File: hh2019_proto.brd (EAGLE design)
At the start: 263.1 x 150 mm, 146 parts, among them IC1 CP210X_USB_UART, IC2 AP2114H, IC4 TP4056, J1 PJ-313D, Q1 MMBT2222A, Q3 MMBT2222A, Q4 MMBT2222A, Q5 SI1304 BDL, U1 MPR121QR2, U2 ESP32-WROVER-I, U3 PCM5102A, X4 JST-PH3

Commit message: Placed major components, working on passives
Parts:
- removed C31: 100n, hh2019_proto:C0603-DASHES
- moved Q3 265.5 mm to (-135.9, 67.3)
- moved R22 262.2 mm to (-133.3, 64.8), turned to 180 degrees
- moved R16 261.1 mm to (-133.3, 73.7), turned to 0 degrees
- moved R15 258.0 mm to (-138.4, 69.8), turned to 90 degrees
- moved R18 255.2 mm to (-133.3, 69.8), turned to 270 degrees
- moved Q4 253.3 mm to (-135.9, 72.4), turned to 0 degrees
- moved IC4 252.3 mm to (-104.1, 74.9), turned to 180 degrees
- moved C28 223.6 mm to (-135.9, 99.1), turned to 90 degrees
- moved C29 216.0 mm to (-134.6, 99.1), turned to 90 degrees
- moved C37 190.2 mm to (135.9, 130.8)
- moved R20 190.2 mm to (135.9, 138.4)
- moved R21 190.2 mm to (135.9, 142.2)
- moved C16 190.2 mm to (137.2, 138.4)
- moved C38 190.2 mm to (143.5, 129.5)
- moved C39 190.2 mm to (153.7, 120.7)
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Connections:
- net GND: no longer C31.1
- net N$43: no longer C31.2
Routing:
- net WS2812_POWER: track 0.00 -> 68.8 mm
- net ESP32_FLASH: track 0.00 -> 60.5 mm, vias 0 -> 2
- net CHRG_STAT: track 4.52 -> 44.3 mm, vias 2 -> 4
- net GND: track 23.2 -> 61.7 mm, vias 7 -> 28
- net VBAT: track 0.00 -> 25.9 mm
- net WS2812_DATA: track 0.00 -> 23.8 mm, vias 0 -> 2
- net USB_DP_CON: track 0.00 -> 12.9 mm, vias 0 -> 2
- net USB_DN_CON: track 0.00 -> 11.7 mm
- net N$4: track 0.00 -> 9.75 mm
- net N$3: track 0.00 -> 9.75 mm
- net N$2: track 0.00 -> 9.75 mm
- net N$19: track 0.00 -> 9.75 mm
- net N$43: track 0.00 -> 9.15 mm
- net N$42: track 0.00 -> 8.39 mm
- net N$53: track 0.00 -> 7.33 mm
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
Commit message: Routing tracks
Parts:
- moved C27 369.4 mm to (-101.7, 78.8), turned to 0 degrees
- moved C22 366.0 mm to (-102.8, 81.4), turned to 270 degrees
- moved C17 359.8 mm to (-102.8, 85.2), turned to 270 degrees
- moved C26 354.5 mm to (-102.8, 90.2), turned to 270 degrees
- moved C30 349.1 mm to (-102.8, 95.3), turned to 270 degrees
- moved IC2 337.7 mm to (-97.8, 92.8), turned to 0 degrees
- moved C15 334.1 mm to (-97.8, 86.4), turned to 180 degrees
- moved C14 331.6 mm to (-97.8, 83.9), turned to 180 degrees
- moved C18 329.4 mm to (-97.8, 80.8), turned to 180 degrees
- moved R19 274.3 mm to (-121.9, 129.5)
- moved C19 270.5 mm to (-119.4, 129.5)
- moved C21 266.7 mm to (-116.8, 129.5)
- moved C33 262.9 mm to (-114.3, 129.5)
- moved C36 259.1 mm to (-114.3, 125.7)
- moved C32 259.1 mm to (-111.8, 129.5)
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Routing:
- net GND: track 61.7 -> 92.4 mm, vias 28 -> 33
- net VCC: track 2.85 -> 31.5 mm, vias 0 -> 2
- net VGH: track 0.00 -> 16.6 mm, vias 0 -> 2
- net VGL: track 0.00 -> 13.5 mm, vias 0 -> 2
- net VSL: track 0.00 -> 10.1 mm
- net VCOM: track 0.00 -> 9.84 mm, vias 0 -> 2
- net PREVGL: track 0.00 -> 8.85 mm, vias 0 -> 2
- net PREVGH: track 0.00 -> 8.55 mm
- net RESE: track 0.00 -> 8.42 mm, vias 0 -> 2
- net VSH: track 0.00 -> 6.55 mm
- net VBAT: track 25.9 -> 20.0 mm, vias 0 -> 2
- net +5V: track 0.00 -> 5.56 mm
- net ESP32_FLASH: track 60.5 -> 61.6 mm
- net ESP32_!RESET: track 44.4 -> 45.5 mm, vias 0 -> 2
- net I2C_SDA: track 69.4 -> 70.3 mm
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
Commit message: Added most non-bypass passives
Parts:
- moved Q5 270.6 mm to (-115.6, 121.9), turned to 270 degrees
- moved C23 264.3 mm to (-113.0, 86.4), turned to 0 degrees
- moved C24 264.0 mm to (-113.0, 82.5), turned to 180 degrees
- moved R30 262.7 mm to (-113.0, 78.7), turned to 0 degrees
- moved R32 262.5 mm to (-113.0, 74.9), turned to 0 degrees
- moved L1 261.8 mm to (-106.8, 120.0)
- moved R29 258.6 mm to (-110.5, 66.0), turned to 180 degrees
- moved R35 258.6 mm to (-110.5, 63.5), turned to 0 degrees
- moved SJ3 258.6 mm to (-110.5, 61.0), turned to 180 degrees
- moved C25 257.8 mm to (-106.7, 124.5), turned to 90 degrees
- moved D9 256.6 mm to (-109.2, 129.5)
- moved D8 256.5 mm to (-111.8, 125.7), turned to 90 degrees
- moved D7 252.8 mm to (-110.5, 121.9), turned to 0 degrees
- moved R36 248.2 mm to (-106.7, 68.6), turned to 0 degrees
- moved C34 244.9 mm to (-97.4, 78.0), turned to 0 degrees
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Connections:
- new net BAT: C34.1, F2.1, IC4.5, X4.3
- net VBAT: no longer C34.1, F2.1, IC4.5, X4.3
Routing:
- net +5V: track 5.56 -> 108.2 mm, vias 0 -> 4
- net N$50: track 0.00 -> 78.4 mm, vias 0 -> 4
- net N$11: track 0.00 -> 69.5 mm, vias 0 -> 4
- net N$10: track 0.00 -> 65.3 mm, vias 0 -> 4
- net WS2812_POWER: track 68.8 -> 132.2 mm, vias 0 -> 4
- net I2S_SCK: track 0.00 -> 51.5 mm, vias 0 -> 2
- net ESP32_TX: track 5.49 -> 46.1 mm, vias 0 -> 2
- net ESP32_RX: track 5.78 -> 44.6 mm, vias 0 -> 2
- net I2S_SD: track 0.00 -> 37.9 mm, vias 0 -> 2
- net I2S_WS: track 0.00 -> 36.6 mm, vias 0 -> 2
- net GND: track 92.4 -> 126.3 mm, vias 33 -> 43
- net I2C_INT: track 68.4 -> 98.2 mm
- net LCD_VDD: track 0.00 -> 18.7 mm, vias 0 -> 2
- net ESP32_FLASH: track 61.6 -> 80.2 mm
- net BAT: track 0.00 -> 18.6 mm, vias 0 -> 2
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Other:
- board text removed: "+3V3"
- board text removed: "3V3_SWITCHED"
- board text removed: "ESP32_!RESET"
- board text removed: "ESP32_FLASH"
- board text removed: "I2C_SCL"
- board text removed: "I2C_SDA"
- board text removed: "WS2812_POWER"

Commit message: All but the last handful passives placed and routed
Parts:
- moved C16 173.1 mm to (-111.8, 95.2), turned to 270 degrees
- moved R20 168.1 mm to (-109.2, 95.2), turned to 90 degrees
- moved R21 163.1 mm to (-106.7, 95.2), turned to 270 degrees
- moved R23 153.1 mm to (-113.0, 100.3)
- moved R24 153.1 mm to (-109.2, 100.3)
- moved R12 149.4 mm to (-109.2, 108.0), turned to 90 degrees
- moved D6 147.0 mm to (-111.8, 108.0), turned to 0 degrees
- moved C9 105.6 mm to (-146.1, 133.3), turned to 270 degrees
- moved D1 102.9 mm to (-146.1, 138.4)
- moved C11 98.5 mm to (-146.1, 128.3), turned to 270 degrees
- moved C20 95.3 mm to (-22.9, 94.0)
- moved C37 95.3 mm to (-40.6, 109.2)
- moved C39 95.3 mm to (-22.9, 99.1)
- moved C40 95.3 mm to (-57.1, 99.1)
- moved C46 95.3 mm to (-22.9, 96.5)
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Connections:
- net N$8 renamed RST
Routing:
- net VDD: track 14.9 -> 87.5 mm, vias 2 -> 7
- net VBAT_SENSE: track 0.00 -> 35.9 mm
- net GND: track 126.3 -> 160.1 mm, vias 43 -> 51
- net VUSB_SENSE: track 0.00 -> 25.5 mm, vias 0 -> 2
- net GDR: track 0.00 -> 24.9 mm, vias 0 -> 2
- net RESE: track 8.42 -> 29.4 mm, vias 2 -> 4
- net +5V: track 108.2 -> 126.8 mm
- net LDO0: track 0.00 -> 15.3 mm, vias 0 -> 2
- net VBAT: track 3.79 -> 18.4 mm
- net VNEG: track 0.00 -> 14.3 mm, vias 0 -> 2
- net I2C_SCL: track 68.7 -> 80.9 mm, vias 2 -> 3
- net CAPP: track 0.00 -> 10.3 mm
- net CAPM: track 0.00 -> 9.82 mm
- net I2C_SDA: track 70.3 -> 78.7 mm, vias 2 -> 3
- net BAT: track 18.6 -> 25.8 mm
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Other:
- board text added: "Power"

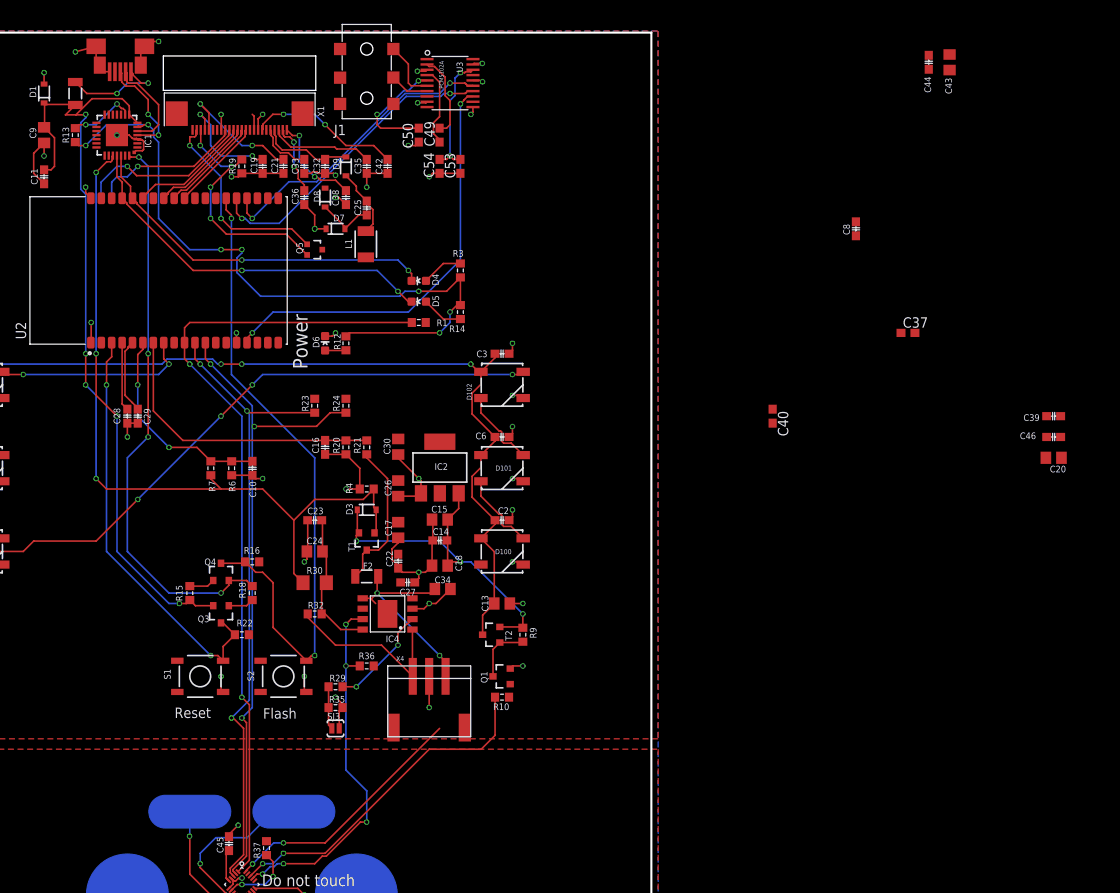
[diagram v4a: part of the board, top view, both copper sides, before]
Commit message: All components placed
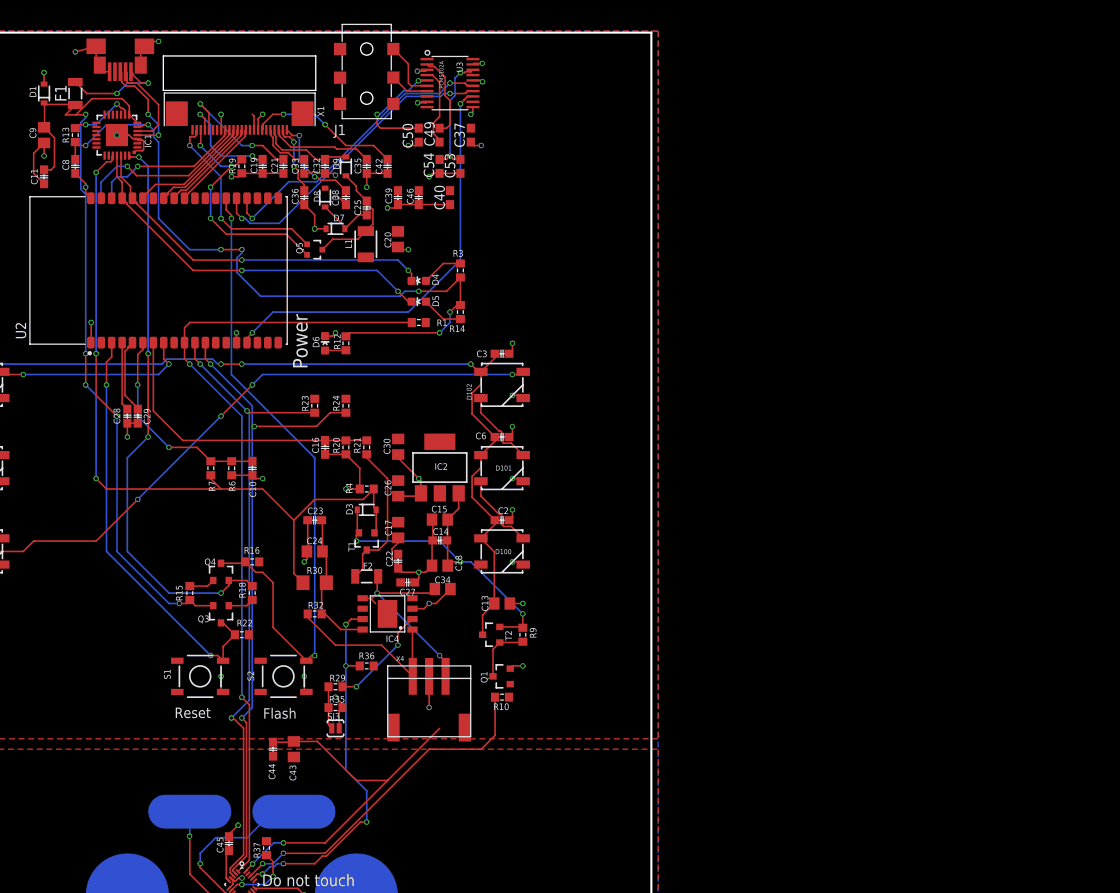
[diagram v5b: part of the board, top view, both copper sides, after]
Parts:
- moved C43 115.9 mm to (-115.6, 58.4)
- moved C44 115.9 mm to (-118.1, 58.4)
- moved C8 95.6 mm to (-142.2, 129.5), turned to 270 degrees
- moved C20 84.3 mm to (-102.9, 120.7), turned to 270 degrees
- moved C39 84.3 mm to (-102.9, 125.7), turned to 270 degrees
- moved C46 82.8 mm to (-100.3, 125.7), turned to 270 degrees
- moved C37 58.5 mm to (-94.0, 133.3), turned to 90 degrees
- moved C40 47.6 mm to (-96.5, 125.7), turned to 90 degrees
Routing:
- net 3V3: track 32.9 -> 48.9 mm
- net GND: track 160.1 -> 172.9 mm, vias 51 -> 54
- net N$23: track 8.47 -> 14.7 mm
- net VDD: track 87.5 -> 89.7 mm
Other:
- board text added: "F1"

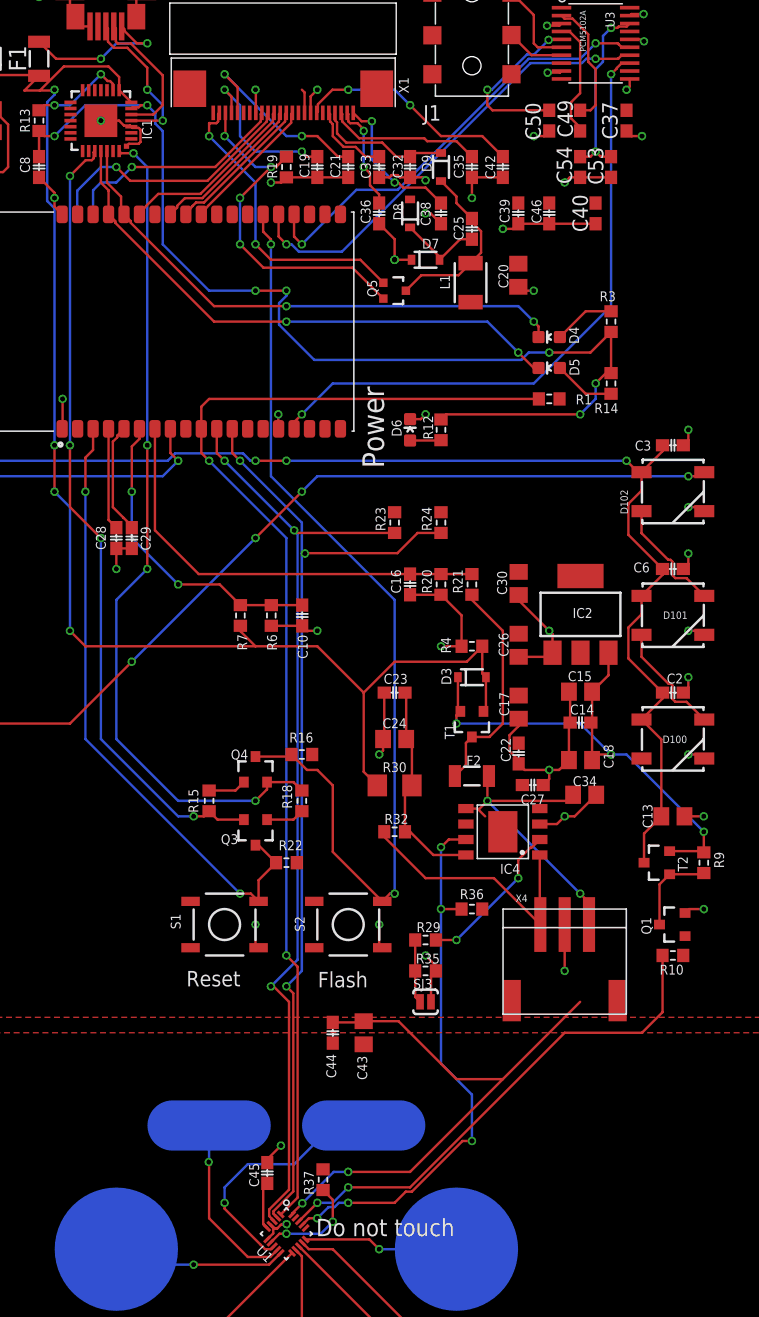
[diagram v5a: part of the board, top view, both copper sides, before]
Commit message: Fixed DRC errors
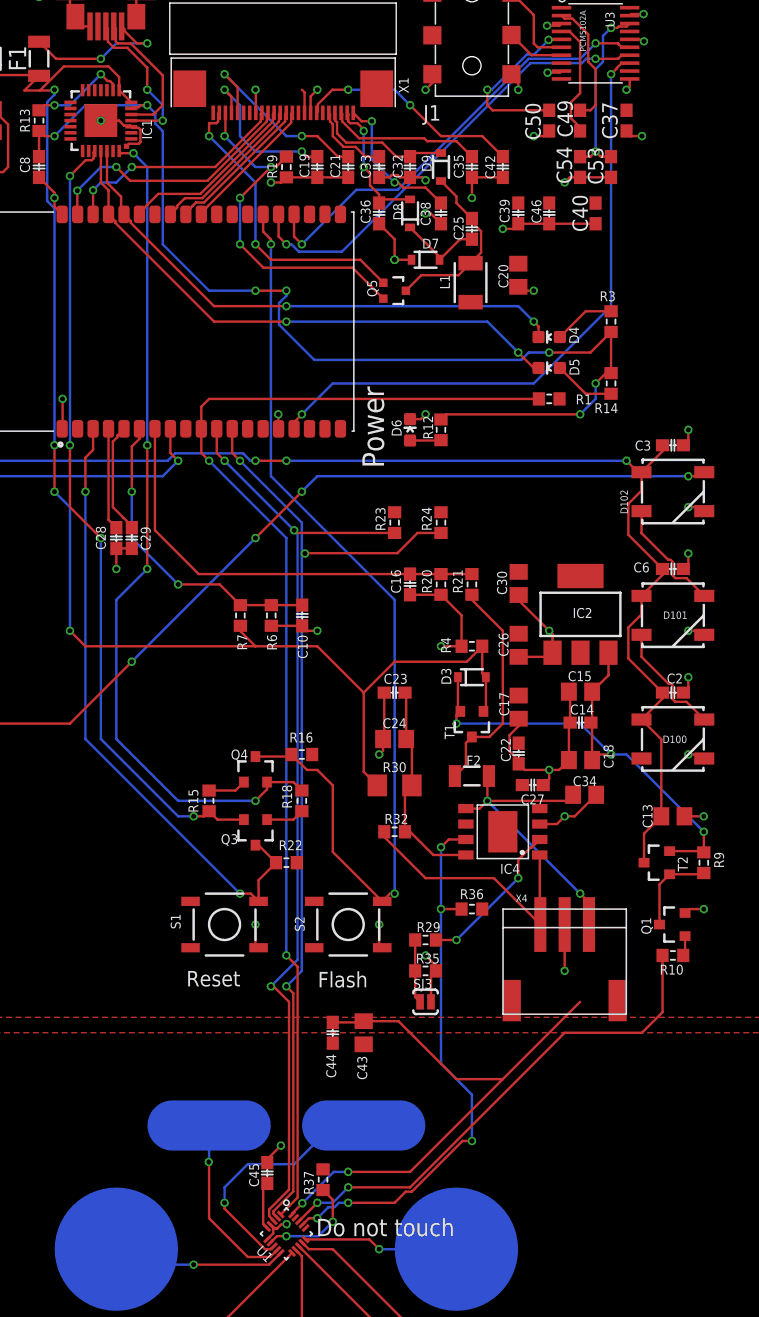
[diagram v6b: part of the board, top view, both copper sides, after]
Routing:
- net GND: track 172.9 -> 175.9 mm, vias 54 -> 56
- net PREVGL: track 8.85 -> 11.5 mm
- net N$52: track 0.00 -> 1.65 mm
- net BAT: track 25.8 -> 25.0 mm
- net LCD_BUSY: track 18.9 -> 18.8 mm, vias 1 -> 2
- net LCD_!RESET: vias 1 -> 2
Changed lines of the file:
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@@
 <via x="-104.14" y="124.46" extent="1-16" drill="0.4"/>
 <wire x1="-96.52" y1="124.88" x2="-100.33" y2="124.88" width="0.2" layer="1"/>
+<wire x1="-103.43" y1="137.16" x2="-102.87" y2="136.6" width="0.2" layer="1"/>
+<wire x1="-102.87" y1="136.6" x2="-102.87" y2="135.89" width="0.2" layer="1"/>
+<via x="-102.87" y="135.89" extent="1-16" drill="0.4"/>
+<wire x1="-109.93" y1="137.16" x2="-109.93" y2="136.45" width="0.2" layer="1"/>
+<wire x1="-109.93" y1="136.45" x2="-110.49" y2="135.89" width="0.2" layer="1"/>
+<via x="-110.49" y="135.89" extent="1-16" drill="0.4"/>
 <wire x1="123.19" y1="72.39" x2="133.35" y2="72.39" width="0" layer="19" extent="1-1"/>
 <wire x1="114.3" y1="72.39" x2="123.19" y2="72.39" width="0" layer="19" extent="1-1"/>
@@
 <wire x1="95.25" y1="20.32" x2="104.14" y2="20.32" width="0" layer="19" extent="1-1"/>
 <wire x1="-87.63" y1="76.2" x2="95.25" y2="72.39" width="0" layer="19" extent="1-1"/>
-<wire x1="-103.43" y1="137.16" x2="-100.464446875" y2="137.294446875" width="0" layer="19" extent="1-1"/>
-<wire x1="-109.93" y1="137.16" x2="-103.43" y2="137.16" width="0" layer="19" extent="1-1"/>
 </signal>
 <signal name="USB_DN_CON">
@@
 <wire x1="-135.89" y1="128.27" x2="-137.16" y2="128.27" width="0.2" layer="16"/>
 <wire x1="-137.16" y1="128.27" x2="-137.8" y2="127.63" width="0.2" layer="16"/>
-<wire x1="-137.8" y1="127.63" x2="-137.8" y2="125.6" width="0.2" layer="16"/>
 <wire x1="-124.0276" y1="133.2822" x2="-127.7698" y2="129.54" width="0.2" layer="1"/>
-<wire x1="-137.8" y1="125.6" x2="-137.8" y2="125.65" width="0" layer="19" extent="1-16"/>
+<via x="-137.8" y="127.63" extent="1-16" drill="0.4"/>
+<wire x1="-137.8" y1="127.63" x2="-137.8" y2="125.65" width="0.2" layer="1"/>
 </signal>
 <signal name="LCD_!RESET">
@@
 <via x="-135.89" y="129.54" extent="1-16" drill="0.4"/>
 <wire x1="-135.89" y1="129.54" x2="-137.16" y2="129.54" width="0.2" layer="16"/>
-<wire x1="-139.1" y1="127.6" x2="-139.1" y2="125.6" width="0.2" layer="16"/>
 <wire x1="-137.16" y1="129.54" x2="-139.1" y2="127.6" width="0.2" layer="16"/>
-<wire x1="-139.1" y1="125.6" x2="-139.07" y2="125.65" width="0" layer="19" extent="1-16"/>
+<wire x1="-139.1" y1="127.6" x2="-139.0952" y2="127.6" width="0.2" layer="16"/>
+<via x="-139.0952" y="127.6" extent="1-16" drill="0.4"/>
+<wire x1="-139.0952" y1="127.6" x2="-139.0952" y2="125.6752" width="0.2" layer="1"/>
+<wire x1="-139.0952" y1="125.6752" x2="-139.07" y2="125.65" width="0.2" layer="1"/>
 </signal>
 <signal name="LCD_CS">
@@
 <wire x1="-114.3" y1="127.28305" x2="-114.3" y2="126.58" width="0.2" layer="1"/>
 <wire x1="-115.0524" y1="128.03545" x2="-114.3" y2="127.28305" width="0.2" layer="1"/>
-<wire x1="-114.3" y1="126.58" x2="-111.76" y2="126.88" width="0" layer="19" extent="1-1"/>
+<wire x1="-114.3" y1="126.58" x2="-114" y2="126.88" width="0.2" layer="1"/>
+<wire x1="-114" y1="126.88" x2="-111.76" y2="126.88" width="0.2" layer="1"/>
 </signal>
 <signal name="VCOM">
@@
 <contactref element="Q1" pad="1"/>
 <contactref element="R10" pad="2"/>
-<wire x1="-89.17" y1="66.36" x2="-89.32" y2="64.77" width="0" layer="19" extent="1-1"/>
+<wire x1="-89.17" y1="66.36" x2="-89.17" y2="64.92" width="0.2" layer="1"/>
+<wire x1="-89.17" y1="64.92" x2="-89.32" y2="64.77" width="0.2" layer="1"/>
 </signal>
 <signal name="N$53">
@@
 <contactref element="U1" pad="5"/>
 <contactref element="C45" pad="1"/>
-<wire x1="-123.500525" y1="42.376971875" x2="-123.8" y2="42.676446875" width="0.2" layer="1"/>
 <wire x1="-123.500525" y1="42.376971875" x2="-123.500525" y2="42.379240625" width="0.2" layer="1"/>
 <wire x1="-123.500525" y1="42.379240625" x2="-123.8247625" y2="42.703478125" width="0.2" layer="1"/>
@@
 <contactref element="U1" pad="7"/>
 <contactref element="R37" pad="2"/>
-<wire x1="-123.231115625" y1="41.17361875" x2="-122.494734375" y2="41.91" width="0.2" layer="1"/>
-<wire x1="-122.494734375" y1="41.91" x2="-121.92" y2="41.91" width="0.2" layer="1"/>
-<via x="-121.92" y="41.91" extent="1-16" drill="0.4"/>
-<wire x1="-121.92" y1="41.91" x2="-119.09543125" y2="41.91" width="0.2" layer="16"/>
-<wire x1="-119.09543125" y1="41.91" x2="-118.11" y2="42.89543125" width="0.2" layer="16"/>
+<wire x1="-123.231115625" y1="41.17361875" x2="-122.694734375" y2="41.71" width="0.2" layer="1"/>
+<wire x1="-122.694734375" y1="41.71" x2="-121.92" y2="41.71" width="0.2" layer="1"/>
+<via x="-121.92" y="41.71" extent="1-16" drill="0.4"/>
+<wire x1="-121.92" y1="41.71" x2="-119.29543125" y2="41.71" width="0.2" layer="16"/>
+<wire x1="-119.29543125" y1="41.71" x2="-118.11" y2="42.89543125" width="0.2" layer="16"/>
 <via x="-118.11" y="42.89543125" extent="1-16" drill="0.4"/>
 <wire x1="-118.11" y1="42.89543125" x2="-118.11" y2="44.7" width="0.2" layer="1"/>
@@
 <contactref element="C34" pad="1"/>
 <contactref element="IC4" pad="5"/>
-<wire x1="-105.5924" y1="76.2" x2="-106.1362" y2="76.7438" width="0.2" layer="1"/>
-<wire x1="-106.1362" y1="76.7438" x2="-106.2274" y2="76.835" width="0.2" layer="1"/>
-<wire x1="-106.2274" y1="76.835" x2="-107.175" y2="76.835" width="0.2" layer="1"/>
 <wire x1="-97.06" y1="67.31" x2="-97.06" y2="69.12" width="0.2" layer="1"/>
 <wire x1="-97.06" y1="69.12" x2="-97.79" y2="69.85" width="0.2" layer="1"/>
@@
 <wire x1="-97.79" y1="69.85" x2="-105.41" y2="77.47" width="0.2" layer="16"/>
 <via x="-105.41" y="77.47" extent="1-16" drill="0.4"/>
-<wire x1="-105.41" y1="77.47" x2="-106.1362" y2="76.7438" width="0.2" layer="1"/>
 <contactref element="F2" pad="1"/>
 <wire x1="-105.28" y1="79.51" x2="-105.41" y2="79.38" width="0.2" layer="1"/>
@@
 <wire x1="-98.37" y1="77.97" x2="-98.87" y2="77.47" width="0.2" layer="1"/>
 <wire x1="-98.87" y1="77.47" x2="-105.41" y2="77.47" width="0.2" layer="1"/>
+<wire x1="-105.41" y1="77.47" x2="-106.045" y2="76.835" width="0.2" layer="1"/>
+<wire x1="-106.045" y1="76.835" x2="-107.175" y2="76.835" width="0.2" layer="1"/>
 </signal>
 </signals>
@@
 <mfgpreviewcolor name="substratecolor" color="0xFF786E46"/>
 </mfgpreviewcolors>
+<errors>
+</errors>
 </board>
 </drawing>
